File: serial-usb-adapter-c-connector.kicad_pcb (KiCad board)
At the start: 2 copper layers, 38 x 26 mm, 31 parts, among them J1 USB_C_Receptacle_USB2.0, J2 UART Header, U1 LPC47M192, U2 FT231XS, Y1 SG5032CAN 14.318MHz

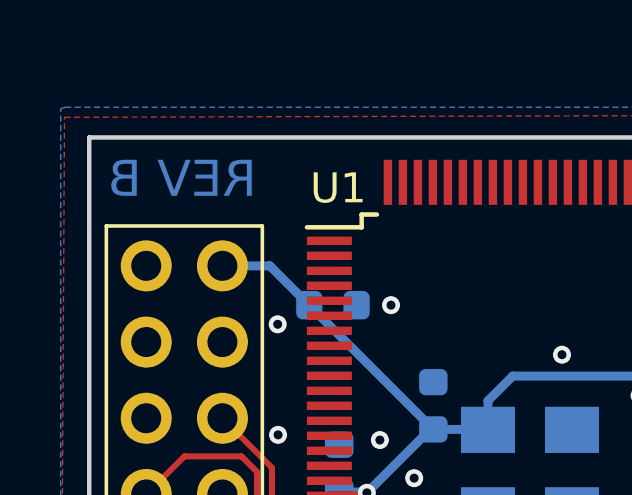
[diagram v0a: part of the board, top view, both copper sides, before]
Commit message: Fixed FB1 position in schematic
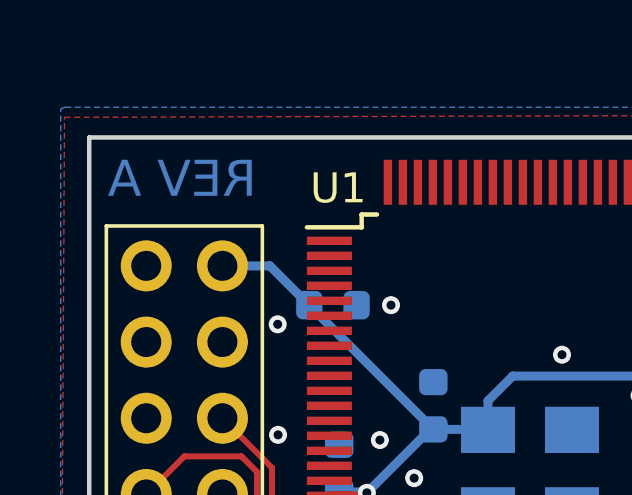
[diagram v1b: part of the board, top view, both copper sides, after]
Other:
- board text added: "REV A"
- board text removed: "REV B"
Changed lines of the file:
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@@
     (title "Original Xbox Serial USB Adapter")
     (date 2019-03-27)
-    (rev B)
+    (rev A)
     (company XboxDev)
     (comment 2 "Copyright Mike Davis 2019")
@@
   )
   (layers
-    (0 F.Cu signal)
-    (31 B.Cu signal hide)
+    (0 F.Cu signal hide)
+    (31 B.Cu signal)
     (32 B.Adhes user hide)
     (33 F.Adhes user hide)
@@
     (effects (font (size 1 1) (thickness 0.153)))
   )
-  (gr_text "REV B" (at 95.90278 108.84662) (layer B.Cu)
+  (gr_text "REV A" (at 95.90278 108.84662) (layer B.Cu)
     (effects (font (size 1.2 1.2) (thickness 0.2)) (justify mirror))
   )
